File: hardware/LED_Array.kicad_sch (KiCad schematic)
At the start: 30 parts, among them J2 Status_LED_Header, J3 HP_LED_Header, U5 PT4115, U6 PT4115, U7 PT4115, U8 PT4115

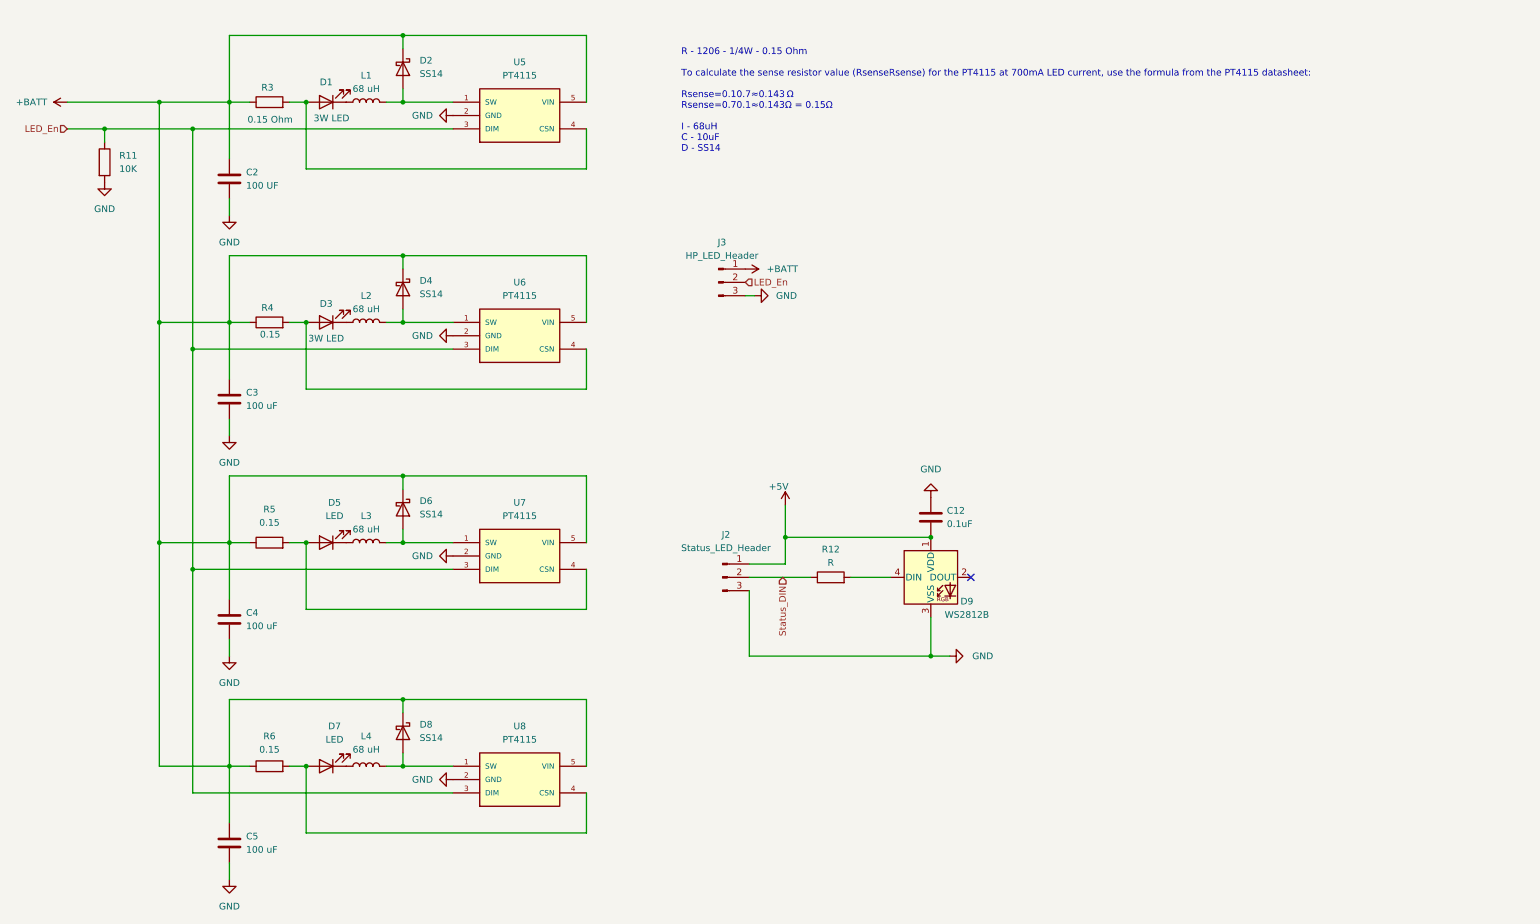
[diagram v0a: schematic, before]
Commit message: Hardware V0.2 - Schematics update
Combines Cell holder, BMS, and voltage regulator into single board
complete w. extensive electrical and thermal protections including:

* MM3220 BMS w Overvoltage, Overcurrent, undervoltage charging/discharge protect
* Fuses on cells, 12v in, 5v and 8.4v out.
* Reverse polarity protection on 12v and cells.

Adds debug UART header
Single IO header on every board
Minor component size corrections
Add current limiting resistor to RPI power NMOS gate.
Add optional support for MLCC/tantalum caps for Voltage Regulator instead of electrolytic
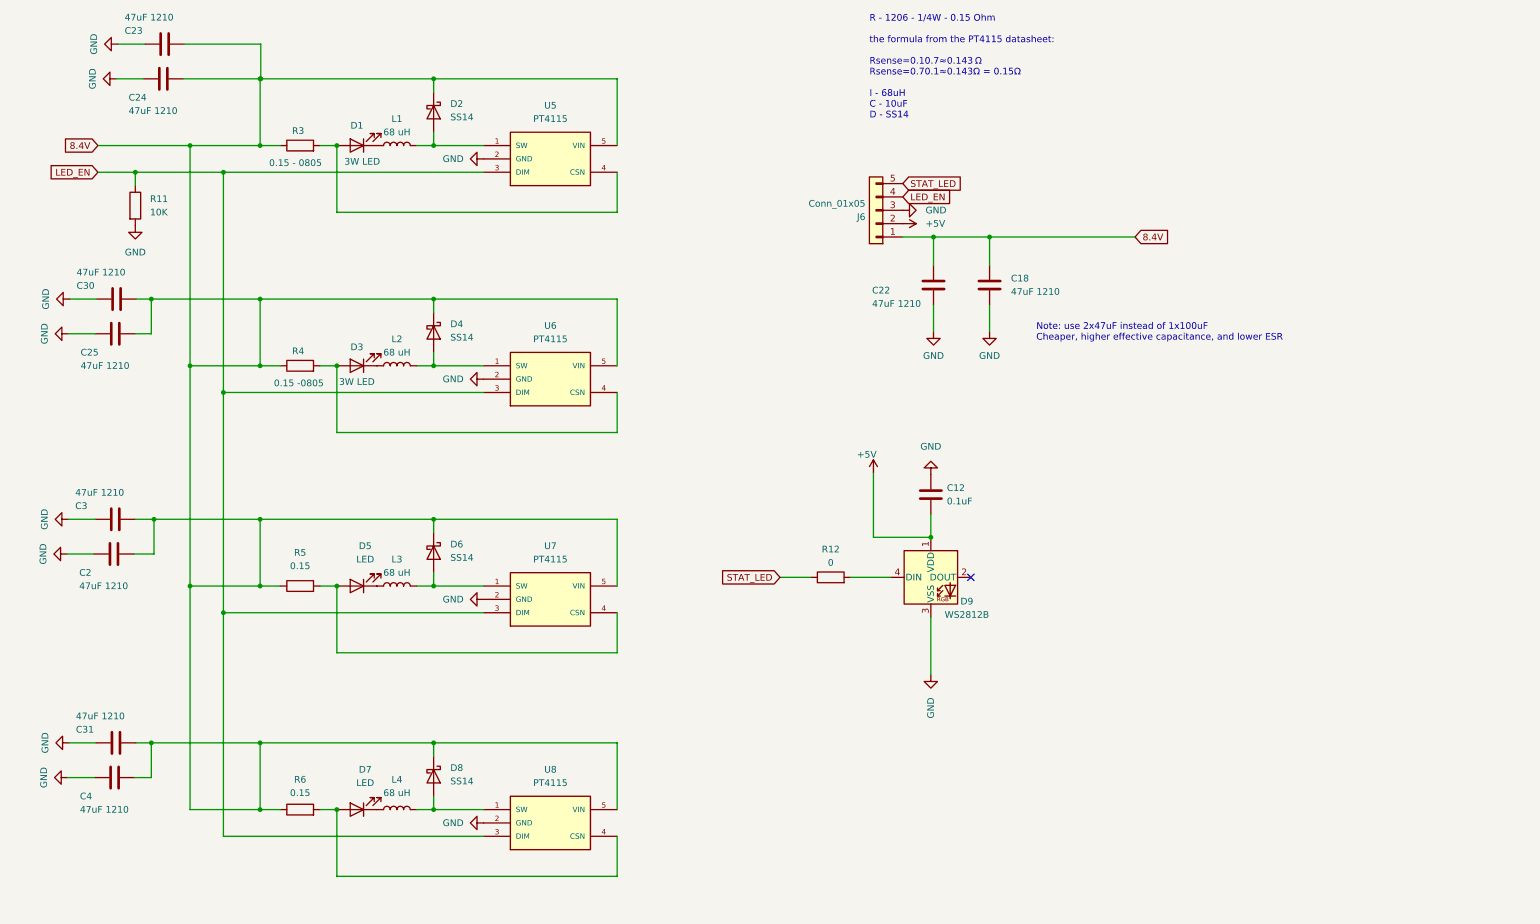
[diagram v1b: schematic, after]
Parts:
- removed C5: 100 uF, Capacitor_SMD:C_0504_1310Metric_Pad0.83x1.28mm_HandSolder, symbol Device:C
- removed J2: Status_LED_Header, Connector_PinHeader_2.54mm:PinHeader_1x03_P2.54mm_Vertical, symbol Connector:Conn_01x03_Pin
- removed J3: HP_LED_Header, Connector_PinSocket_2.54mm:PinSocket_1x03_P2.54mm_Vertical, symbol Connector:Conn_01x03_Pin
- added C18, C22, C23, C24, C25, C30, C31: 47uF 1210, Resistor_SMD:R_1210_3225Metric_Pad1.30x2.65mm_HandSolder, symbol Device:C
- added J6: Conn_01x05, Connector_PinSocket_2.54mm:PinSocket_1x05_P2.54mm_Vertical, symbol Connector_Generic:Conn_01x05
- C12: footprint Capacitor_SMD:C_0504_1310Metric_Pad0.83x1.28mm_HandSolder -> Capacitor_SMD:C_0603_1608Metric_Pad1.08x0.95mm_HandSolder
- C2: value 100 UF -> 47uF 1210; footprint Capacitor_SMD:C_0504_1310Metric_Pad0.83x1.28mm_HandSolder -> Resistor_SMD:R_1210_3225Metric_Pad1.30x2.65mm_HandSolder
- C3, C4: value 100 uF -> 47uF 1210; footprint Capacitor_SMD:C_0504_1310Metric_Pad0.83x1.28mm_HandSolder -> Resistor_SMD:R_1210_3225Metric_Pad1.30x2.65mm_HandSolder
- L1, L2, L3, L4: footprint Inductor_SMD:L_TDK_VLS6045EX_VLS6045AF -> Inductor - DR74 68uH:DR74
- R12: value R -> 0
- R3: value 0.15 Ohm -> 0.15 - 0805
- R4: value 0.15 -> 0.15 -0805
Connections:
- net +5V: now also J6.2 (Pin_2)
- net GND: now also C18.2, C22.2, C23.2, C24.2, C25.2, C30.2, C31.2, J6.3 (Pin_3)
- net +BATT renamed 8.4V
- net 8.4V: now also C18.1, C22.1, C23.1, C24.1, C25.1, C30.1, C31.1, J6.1 (Pin_1)
- net LED_En renamed LED_EN
- net LED_EN: now also J6.4 (Pin_4)
- net Status_DIN renamed STAT_LED
- net STAT_LED: now also J6.5 (Pin_5)
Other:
- note added: "Note: use 2x47uF instead of 1x100uF Cheaper, higher effective capacitance, and lower ESR"
- note added: "R - 1206 - 1/4W - 0.15 Ohm the formula from the PT4115 datasheet: Rsense=0.10.7≈0.143 Ω Rsense​=0.70.1​≈0.143Ω = 0.15Ω I - 68uH C - 10uF D - SS14"
- note removed: "R - 1206 - 1/4W - 0.15 Ohm To calculate the sense resistor value (RsenseRsense​) for the PT4115 at 700mA LED current, use the formula from the PT4115 datasheet: Rsense=0.10.7≈0.143 Ω Rsense​=0.70.1​≈0.143Ω = 0.15Ω I - 68uH C - 10uF D - SS14"
- moved on the sheet: C12, D1, D2, D3, D4, D5, D6, D7, D8, L1, L2, L3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

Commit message: Hardware revision 0.2 routing
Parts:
- removed J6: Conn_01x05, Connector_PinSocket_2.54mm:PinSocket_1x05_P2.54mm_Vertical, symbol Connector_Generic:Conn_01x05
- added J10, J11, J12, J13, J14, J5, J8, J9: Conn_01x02_Pin, Connector_PinHeader_2.54mm:PinHeader_1x02_P2.54mm_Vertical, symbol Connector:Conn_01x02_Pin
- added J15: LED_Board_Header, Connector_PinHeader_2.54mm:PinHeader_1x03_P2.54mm_Vertical, symbol Connector_Generic:Conn_01x03
- added J6: Conn_01x03, Connector_PinHeader_2.54mm:PinHeader_1x03_P2.54mm_Vertical, symbol Connector_Generic:Conn_01x03
- D1, D3: footprint LEDs:BEAD-3W-W-120-04 -> LEDS - BEAD 3W LED:BEAD-3W-W-120-04
- D2, D4, D6, D8: footprint Diode_SMD:D_SMA-SMB_Universal_Handsoldering -> Diode_SMD:D_SMA_Handsoldering
- D5, D7: value LED -> 3W LED; footprint LEDs:BEAD-3W-W-120-04 -> LEDS - BEAD 3W LED:BEAD-3W-W-120-04
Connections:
- net +5V: now also J15.3 (Pin_3)
- net 8.4V: now also J6.1 (Pin_1)
- net GND: now also J15.2 (Pin_2), J6.2 (Pin_2)
- net LED_EN: now also J6.3 (Pin_3)
- net STAT_LED: now also J15.1 (Pin_1)
- net at L2.1: now also J8.1 (Pin_1); no longer D3.1 (K)
- net at D5.1 (K): now also J13.1 (Pin_1); no longer L3.1
- net at R5.2, U7.4 (CSN): now also J5.2 (Pin_2); no longer D5.2 (A)
- net at R3.2, U5.4 (CSN): now also J10.2 (Pin_2); no longer D1.2 (A)
- net at L4.1: now also J9.1 (Pin_1); no longer D7.1 (K)
- net at R6.2, U8.4 (CSN): now also J9.2 (Pin_2); no longer D7.2 (A)
- net at R4.2, U6.4 (CSN): now also J8.2 (Pin_2); no longer D3.2 (A)
- net at L1.1: now also J10.1 (Pin_1); no longer D1.1 (K)
- new net: D5.2 (A), J13.2 (Pin_2)
- new net: D1.1 (K), J11.1 (Pin_1)
- new net: D1.2 (A), J11.2 (Pin_2)
- new net: J5.1 (Pin_1), L3.1
- new net: D7.1 (K), J14.1 (Pin_1)
- new net: D7.2 (A), J14.2 (Pin_2)
- new net: D3.1 (K), J12.1 (Pin_1)
- new net: D3.2 (A), J12.2 (Pin_2)
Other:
- company: (none) -> KBader94
- title: (none) -> OpenActionCam
- moved on the sheet: D2, D4, D6, D8, L1, L2, L3, L4, U5, U6, U7, U8
